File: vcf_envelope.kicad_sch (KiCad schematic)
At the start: 19 parts, among them Q2 BC237, U15 4066, U8 4001, U9 Opamp_Dual

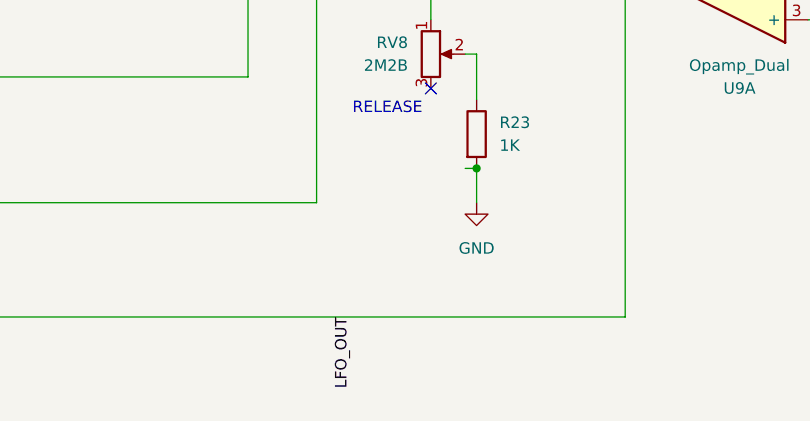
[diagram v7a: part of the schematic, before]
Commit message: Fixed VCF TRIG/GATE net, routed all except keyboard
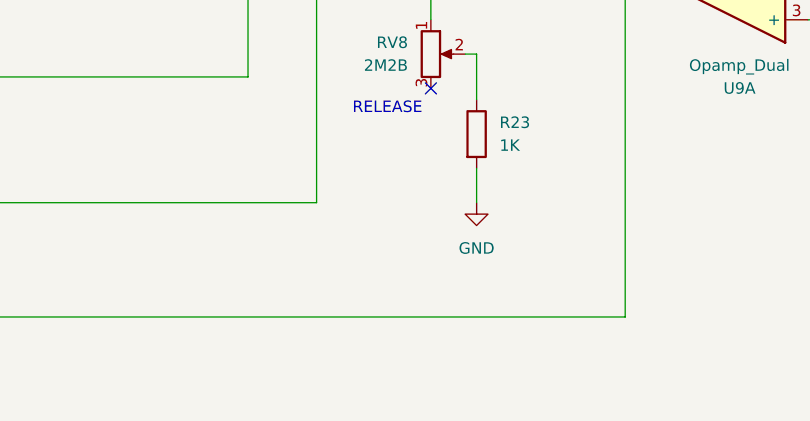
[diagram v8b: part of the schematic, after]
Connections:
- net LFO_OUT: no longer names the net of R22.2, U9.1
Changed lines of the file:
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@@
-	)
-	(junction
-		(at 176.53 140.97)
-		(diameter 0)
-		(color 0 0 0 0)
 	)
 	(junction
@@
 	(wire
 		(pts
+			(xy 71.12 137.16) (xy 73.66 137.16)
+		)
+		(stroke
+			(width 0)
+			(type default)
+		)
+	)
+	(wire
+		(pts
 			(xy 30.48 38.1) (xy 38.1 38.1)
 		)
@@
 	(wire
 		(pts
+			(xy 73.66 137.16) (xy 73.66 133.35)
+		)
+		(stroke
+			(width 0)
+			(type default)
+		)
+	)
+	(wire
+		(pts
 			(xy 99.06 81.28) (xy 99.06 116.84)
 		)
@@
 	(wire
 		(pts
-			(xy 176.53 140.97) (xy 175.26 140.97)
-		)
-		(stroke
-			(width 0)
-			(type default)
-		)
-	)
-	(wire
-		(pts
 			(xy 171.45 88.9) (xy 171.45 99.06)
 		)
@@
 	(wire
 		(pts
-			(xy 71.12 137.16) (xy 73.66 137.16)
-		)
-		(stroke
-			(width 0)
-			(type default)
-		)
-	)
-	(wire
-		(pts
 			(xy 99.06 116.84) (xy 99.06 128.27)
 		)
@@
 		(pts
 			(xy 99.06 144.78) (xy 158.75 144.78)
-		)
-		(stroke
-			(width 0)
-			(type default)
-		)
-	)
-	(wire
-		(pts
-			(xy 73.66 137.16) (xy 73.66 133.35)
 		)
 		(stroke
@@
 	(label "GATE"
 		(at 71.12 137.16 180)
-		(effects
-			(font
-				(size 1.27 1.27)
-			)
-			(justify right bottom)
-		)
-	)
-	(label "LFO_OUT"
-		(at 162.56 157.48 270)
 		(effects
 			(font
@@
 		)
 	)
+	(hierarchical_label "-12V"
+		(shape input)
+		(at 30.48 49.53 180)
+		(effects
+			(font
+				(size 1.27 1.27)
+			)
+			(justify right)
+		)
+	)
 	(hierarchical_label "GATE"
 		(shape input)
@@
 		(effects
 			(font
-				(size 1.27 1.27)
-			)
-			(justify right)
-		)
-	)
-	(hierarchical_label "-12V"
-		(shape input)
-		(at 30.48 49.53 180)
-		(effects
-			(font
